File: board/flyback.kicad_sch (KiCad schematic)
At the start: 24 parts, among them U1 MP8007, U2 POE70P-50L

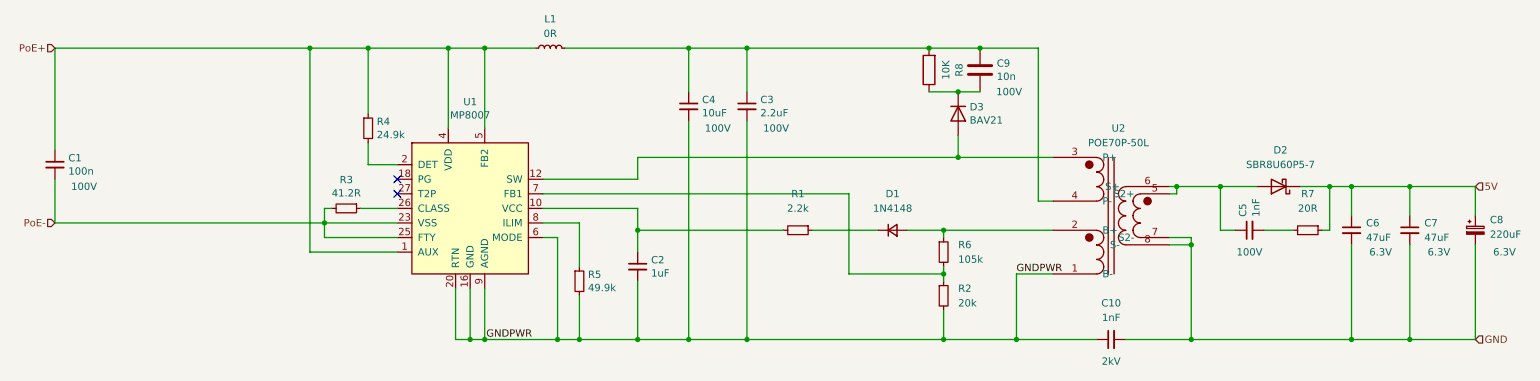
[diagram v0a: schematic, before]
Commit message: improved thermal properties of layout
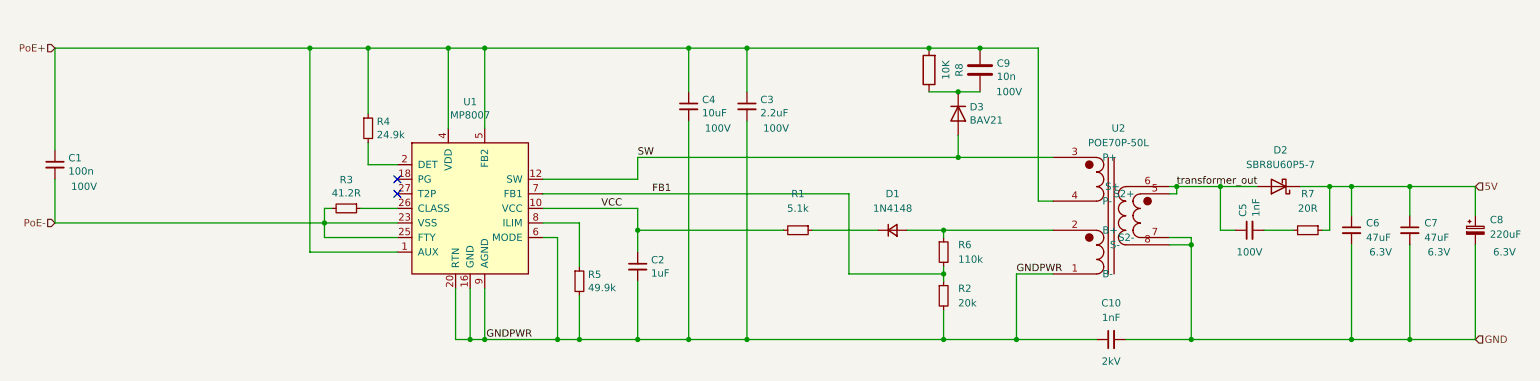
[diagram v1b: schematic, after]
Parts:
- removed L1: 0R, Inductor_SMD:L_1812_4532Metric, symbol Device:L_Small
- R1: value 2.2k -> 5.1k
- R6: value 105k -> 110k
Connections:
- net PoE+: now also C3.1, C4.1, C9.1, R8.2, U2.4 (P-)
- net VCC: now reaches C2.1, R1.2, U1.10 (VCC)
- net SW: now reaches D3.2 (A), U1.12 (SW), U1.13, U2.3 (P+)
- net FB1: now reaches R2.1, R6.2, U1.7 (FB1)
- net transformer_out: now reaches C5.1, D2.2 (A), U2.5 (S2+), U2.6 (S+)
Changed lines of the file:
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@@
-    (stroke (width 0) (type default) (color 0 0 0 0))
-  )
-  (wire (pts (xy 105.41 62.23) (xy 114.3 62.23))
     (stroke (width 0) (type default) (color 0 0 0 0))
   )
@@
     (stroke (width 0) (type default) (color 0 0 0 0))
   )
-  (wire (pts (xy 119.38 62.23) (xy 140.97 62.23))
+  (wire (pts (xy 105.41 62.23) (xy 140.97 62.23))
     (stroke (width 0) (type default) (color 0 0 0 0))
   )
@@
   (wire (pts (xy 132.08 93.98) (xy 132.08 90.17))
     (stroke (width 0) (type default) (color 0 0 0 0))
+  )
+  (label "SW" (at 132.08 81.28 0)
+    (effects (font (size 1.27 1.27)) (justify left bottom))
   )
   (label "GNDPWR" (at 113.665 113.03 180)
     (effects (font (size 1.27 1.27)) (justify right bottom))
+  )
+  (label "VCC" (at 125.73 90.17 0)
+    (effects (font (size 1.27 1.27)) (justify left bottom))
+  )
+  (label "transformer_out" (at 226.06 86.36 0)
+    (effects (font (size 1.27 1.27)) (justify left bottom))
+  )
+  (label "FB1" (at 134.62 87.63 0)
+    (effects (font (size 1.27 1.27)) (justify left bottom))
   )
   (label "GNDPWR" (at 198.12 101.6 0)
@@
     (pin "2")
   )
-  (symbol (lib_id "Device:L_Small") (at 116.84 62.23 90) (unit 1)
-    (in_bom yes) (on_board yes) (fields_autoplaced)
-    (property "Reference" "L1" (id 0) (at 116.84 57.15 90))
-    (property "Value" "0R" (id 1) (at 116.84 59.69 90))
-    (property "Footprint" "Inductor_SMD:L_1812_4532Metric" (id 2) (at 116.84 62.23 0)
-      (effects (font (size 1.27 1.27)) hide)
-    )
-    (property "Datasheet" "~" (id 3) (at 116.84 62.23 0)
-      (effects (font (size 1.27 1.27)) hide)
-    )
-    (pin "1")
-    (pin "2")
-  )
   (symbol (lib_id "Device:R_Small") (at 160.02 93.98 270) (unit 1)
     (in_bom yes) (on_board yes) (fields_autoplaced)
     (property "Reference" "R1" (id 0) (at 160.02 87.63 90))
-    (property "Value" "2.2k" (id 1) (at 160.02 90.17 90))
+    (property "Value" "5.1k" (id 1) (at 160.02 90.17 90))
     (property "Footprint" "Resistor_SMD:R_0603_1608Metric" (id 2) (at 160.02 93.98 0)
       (effects (font (size 1.27 1.27)) hide)
@@
       (effects (font (size 1.27 1.27)) (justify left))
     )
-    (property "Value" "105k" (id 1) (at 187.96 99.0599 0)
-      (effects (font (size 1.27 1.27)) (justify left))
-    )
+    (property "Value" "110k" (id 1) (at 187.96 99.0599 0)
+      (effects (font (size 1.27 1.27)) (justify left))
+    )

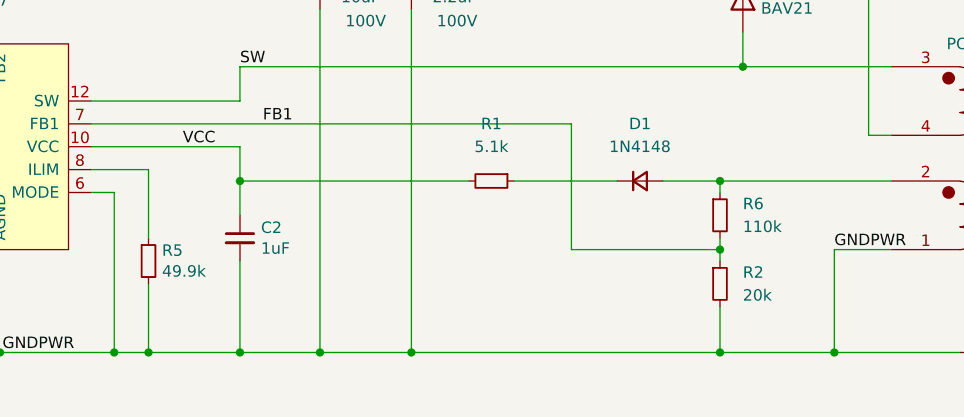
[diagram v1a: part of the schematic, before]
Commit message: updated voltage and current setting resistors
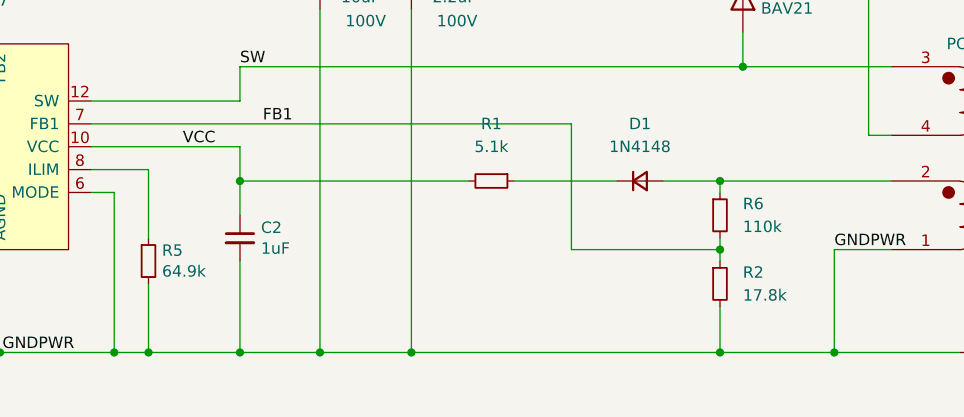
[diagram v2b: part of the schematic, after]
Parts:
- R2: value 20k -> 17.8k
- R5: value 49.9k -> 64.9k
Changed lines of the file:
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@@
       (effects (font (size 1.27 1.27)) (justify left))
     )
-    (property "Value" "49.9k" (id 1) (at 123.4186 104.013 0)
+    (property "Value" "64.9k" (id 1) (at 123.4186 104.013 0)
       (effects (font (size 1.27 1.27)) (justify left))
     )
@@
       (effects (font (size 1.27 1.27)) (justify left))
     )
-    (property "Value" "20k" (id 1) (at 187.96 106.6799 0)
+    (property "Value" "17.8k" (id 1) (at 187.96 106.6799 0)
       (effects (font (size 1.27 1.27)) (justify left))
     )
